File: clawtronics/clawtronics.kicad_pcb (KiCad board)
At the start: 2 copper layers, 81.4 x 87.2 mm, 21 parts, among them J1 TYPE-C-31-M-12, J2 Conn_01x20_Pin, J3 Conn_01x20_Pin, SW1 TS-1088-AR02016, SW2 TS-1088-AR02016, U2 ESP32-S3-WROOM-1, U3 LD1117S33TR_SOT223

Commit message: pcb progress
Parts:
- added C10: 0.1u, Capacitor_SMD:C_0603_1608Metric, F.Cu at (149.5, 76.5)
- added C11: 0.1u, Capacitor_SMD:C_0603_1608Metric, F.Cu at (149.5, 79.0)
- added C12: 0.1u, Capacitor_SMD:C_0603_1608Metric, F.Cu at (149.5, 81.5)
- added C13: 0.1u, Capacitor_SMD:C_0603_1608Metric, F.Cu at (149.5, 84.0)
- added C14: 0.1u, Capacitor_SMD:C_0603_1608Metric, F.Cu at (149.5, 86.5)
- added C15: 0.1u, Capacitor_SMD:C_0603_1608Metric, F.Cu at (153.5, 66.4)
- added C16: 10u, Capacitor_SMD:C_0603_1608Metric, F.Cu at (153.5, 69.0)
- added C17: 0.1u, Capacitor_SMD:C_0603_1608Metric, F.Cu at (153.5, 71.5)
- added C18: 0.1u, Capacitor_SMD:C_0603_1608Metric, F.Cu at (153.5, 74.0)
- added C19: 10u, Capacitor_SMD:C_0603_1608Metric, F.Cu at (153.5, 76.5)
- added C20: 0.022u, Capacitor_SMD:C_0603_1608Metric, F.Cu at (153.5, 79.0)
- added C21: 0.1u, Capacitor_SMD:C_0603_1608Metric, F.Cu at (153.5, 81.5)
- added C22: 0.022u, Capacitor_SMD:C_0603_1608Metric, F.Cu at (153.5, 84.0)
- added C23: 0.022u, Capacitor_SMD:C_0603_1608Metric, F.Cu at (153.5, 86.5)
- added C6: 0.1u, Capacitor_SMD:C_0603_1608Metric, F.Cu at (149.5, 66.4)
- added C7: 0.1u, Capacitor_SMD:C_0603_1608Metric, F.Cu at (149.5, 69.0)
- added C8: 0.1u, Capacitor_SMD:C_0603_1608Metric, F.Cu at (149.5, 71.5)
- added C9: 10u, Capacitor_SMD:C_0603_1608Metric, F.Cu at (149.5, 74.0)
- added J4: Power, Connector_Phoenix_MSTB:PhoenixContact_MSTBV_2,5_6-GF-5,08_1x06_P5.08mm_Vertical_ThreadedFlange_MountHole, F.Cu at (187.5, 78.5)
- added J5: Screw_Terminal_01x06, Connector_Phoenix_MSTB:PhoenixContact_MSTBV_2,5_6-GF-5,08_1x06_P5.08mm_Vertical_ThreadedFlange_MountHole, F.Cu at (122.3, 122.0)
- added R10: 2.74K, Resistor_SMD:R_0603_1608Metric, F.Cu at (157.5, 74.0)
- added R11: 2.21K, Resistor_SMD:R_0603_1608Metric, F.Cu at (157.5, 76.5)
- added R12: 10K, Resistor_SMD:R_0603_1608Metric, F.Cu at (157.5, 79.0)
- added R13: 1K, Resistor_SMD:R_0603_1608Metric, F.Cu at (157.5, 81.5)
- added R14: 2.21K, Resistor_SMD:R_0603_1608Metric, F.Cu at (157.5, 84.0)
- added R15: 10K, Resistor_SMD:R_0603_1608Metric, F.Cu at (157.5, 86.5)
- added R16: 2.74K, Resistor_SMD:R_0603_1608Metric, F.Cu at (161.5, 66.4)
- added R17: 1K, Resistor_SMD:R_0603_1608Metric, F.Cu at (161.5, 69.0)
- added R18: 2.74K, Resistor_SMD:R_0603_1608Metric, F.Cu at (161.5, 71.5)
- added R19: 10K, Resistor_SMD:R_0603_1608Metric, F.Cu at (161.5, 74.0)
- added R20: 10K, Resistor_SMD:R_0603_1608Metric, F.Cu at (161.5, 76.5)
- added R21: 10K, Resistor_SMD:R_0603_1608Metric, F.Cu at (161.5, 79.0)
- added R7: 2.21K, Resistor_SMD:R_0603_1608Metric, F.Cu at (157.5, 66.4)
- added R8: 10K, Resistor_SMD:R_0603_1608Metric, F.Cu at (157.5, 69.0)
- added R9: 1K, Resistor_SMD:R_0603_1608Metric, F.Cu at (157.5, 71.5)
- added U3: DRV8876PWPR, Motors:moto, F.Cu at (181.5, 100.9)
- added U4: DRV8876PWPR, Motors:moto, F.Cu at (167.0, 109.9)
- added U5: DRV8876PWPR, Motors:moto, F.Cu at (145.0, 110.2)
- C1: renamed from C4; value 10u -> 100n
- C5: value 10u -> 1u
- renumbered C1 to C2, C2 to C3, C3 to C4, R2 to R1, R1 to R2, R4 to R3, R5 to R4, R6 to R5, R3 to R6, SW2 to SW1, SW1 to SW2, U2 to U1, U3 to U2

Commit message: figured out switches
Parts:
- removed J1: TYPE-C-31-M-12, TYPE-C-31-M-12:HRO_TYPE-C-31-M-12
- added D4: 1N4001, Diode_THT:D_DO-41_SOD81_P10.16mm_Horizontal, F.Cu at (60.6, 66.6)
- added J6: Screw_Terminal_01x09, TerminalBlock:TerminalBlock_MaiXu_MX126-5.0-09P_1x09_P5.00mm, F.Cu at (30.7, 31.6)
- added J7: Screw_Terminal_01x15, TerminalBlock:TerminalBlock_MaiXu_MX126-5.0-15P_1x15_P5.00mm, F.Cu at (21.5, 21.5)
- added J8: Screw_Terminal_01x02, TerminalBlock:TerminalBlock_MaiXu_MX126-5.0-02P_1x02_P5.00mm, F.Cu at (62.8, 73.7)
- added Q1: AO3400A, Package_TO_SOT_SMD:SOT-23, F.Cu at (75.1, 66.7)
- added R22: 1K, Resistor_SMD:R_0603_1608Metric, F.Cu at (44.7, 63.6)
- added R23: 1K, Resistor_SMD:R_0603_1608Metric, F.Cu at (44.7, 66.1)
- added R24: 1K, Resistor_SMD:R_0603_1608Metric, F.Cu at (44.7, 68.6)
- added R25: 1K, Resistor_SMD:R_0603_1608Metric, F.Cu at (44.7, 71.1)
- added R26: 1K, Resistor_SMD:R_0603_1608Metric, F.Cu at (44.7, 73.6)
- added R27: 660, Resistor_SMD:R_0603_1608Metric, F.Cu at (44.7, 76.2)
- added R28: 220, Resistor_SMD:R_0603_1608Metric, F.Cu at (44.7, 78.7)
- added R29: 10K, Resistor_SMD:R_0603_1608Metric, F.Cu at (44.7, 81.2)
- J2, J3: moved to F.Cu
- J4, J5: footprint Connector_Phoenix_MSTB:PhoenixContact_MSTBV_2,5_6-GF-5,08_1x06_P5.08mm_Vertical_ThreadedFlange_MountHole -> TerminalBlock_MetzConnect:TerminalBlock_MetzConnect_Type011_RT05506HBLC_1x06_P5.00mm_Horizontal
- SW1, SW2: footprint easyeda2kicad:SW-SMD_L3.9-W3.0-P4.45 -> Button_Switch_SMD:SW_SPST_TS-1088-xR020
- moved J4 161.0 mm to (30.2, 44.2), turned to 0 degrees
- moved U3 134.6 mm to (51.6, 65.6)
- moved R10 121.7 mm to (36.7, 88.7)
- moved R7 121.7 mm to (36.7, 81.2)
- moved R8 121.7 mm to (36.7, 83.7)
- moved R9 121.7 mm to (36.7, 86.2)
- moved U4 121.4 mm to (51.6, 72.2)
- moved C10 121.2 mm to (28.7, 86.2)
- moved C11 121.2 mm to (28.7, 88.7)
- moved C6 121.2 mm to (28.7, 76.2)
- moved C7 121.2 mm to (28.7, 78.7)
- moved C8 121.2 mm to (28.7, 81.2)
- moved C9 121.2 mm to (28.7, 83.7)
- moved R16 121.2 mm to (40.7, 76.2)
- moved R17 121.2 mm to (40.7, 78.7)
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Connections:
- C14 pad 2: Net-(U3-VREF) -> Net-(U5-VREF)
- C17 pad 1: Net-(U3-VCP) -> Net-(U5-VCP)
- C20 pad 1: Net-(U5-CPH) -> Net-(U3-CPH)
- C20 pad 2: Net-(U5-CPL) -> Net-(U3-CPL)
- C23 pad 1: Net-(U3-CPH) -> Net-(U5-CPH)
- C23 pad 2: Net-(U3-CPL) -> Net-(U5-CPL)
- C7 pad 2: Net-(U5-VREF) -> Net-(U3-VREF)
- C8 pad 1: Net-(U5-VCP) -> Net-(U3-VCP)
- R10 pad 1: Net-(U5-IPROPI) -> Net-(U3-IPROPI)
- R14 pad 2: Net-(U3-VREF) -> Net-(U5-VREF)
- R15 pad 1: Net-(U3-VREF) -> Net-(U5-VREF)
- R17 pad 2: Net-(U3-IPROPI) -> Net-(U5-IPROPI)
- R18 pad 1: Net-(U3-IPROPI) -> Net-(U5-IPROPI)
- R7 pad 2: Net-(U5-VREF) -> Net-(U3-VREF)
- R8 pad 1: Net-(U5-VREF) -> Net-(U3-VREF)
- R9 pad 2: Net-(U5-IPROPI) -> Net-(U3-IPROPI)
- U3 pad 1: GPIO1 -> GPIO9
- U3 pad 10: Net-(J5-Pin_2) -> Net-(J5-Pin_6)
- U3 pad 2: GPIO2 -> GPIO10
- U3 pad 3: +3V3 -> +3.3V
- U3 pad 8: Net-(J5-Pin_1) -> Net-(J5-Pin_5)
- U5 pad 1: GPIO9 -> GPIO1
- U5 pad 10: Net-(J5-Pin_6) -> Net-(J5-Pin_2)
- U5 pad 2: GPIO10 -> GPIO2
- U5 pad 3: +3.3V -> +3V3
- U5 pad 8: Net-(J5-Pin_5) -> Net-(J5-Pin_1)
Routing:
- net GND: track 114.6 -> 0.00 mm, vias 38 -> 0
- net +5V: track 70.1 -> 0.00 mm, vias 3 -> 0
- net +3V3: track 61.6 -> 0.00 mm, vias 2 -> 0
- net EN: track 59.4 -> 0.00 mm, vias 3 -> 0
- net D-: track 56.2 -> 0.00 mm, vias 2 -> 0
- net D+: track 56.1 -> 0.00 mm, vias 3 -> 0
- net GPIO12: track 36.1 -> 0.00 mm
- net GPIO13: track 35.7 -> 0.00 mm, vias 1 -> 0
- net GPIO0: track 35.3 -> 0.00 mm, vias 1 -> 0
- net GPIO11: track 32.6 -> 0.00 mm
- net GPIO14: track 32.6 -> 0.00 mm, vias 1 -> 0
- net GPIO21: track 30.5 -> 0.00 mm, vias 1 -> 0
- net GPIO10: track 29.6 -> 0.00 mm
- net GPIO9: track 26.5 -> 0.00 mm
- net GPIO47: track 26.5 -> 0.00 mm, vias 1 -> 0
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- removed copper zone on B.Cu, net GND
- removed copper zone on F.Cu, net GND
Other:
- board outline removed
- board text removed: "0"
- board text removed: "1"
- board text removed: "10"
- board text removed: "11"
- board text removed: "12"
- board text removed: "13"
- board text removed: "14"
- board text removed: "15"
- board text removed: "16"
- board text removed: "17"
- board text removed: "18"
- board text removed: "19"
- board text removed: "2"
- board text removed: "20"
- board text removed: "21"
- board text removed: "3"
- board text removed: "35"
- board text removed: "36"
- board text removed: "37"
- board text removed: "38"
- board text removed: "39"
- board text removed: "3V3"
- board text removed: "4"
- board text removed: "40"
- board text removed: "41"
- board text removed: "42"
- board text removed: "43"
- board text removed: "44"
- board text removed: "45"
- board text removed: "46"
- board text removed: "47"
- board text removed: "48"
- board text removed: "5"
- board text removed: "5V"
- board text removed: "6"
- board text removed: "7"
- board text removed: "8"
- board text removed: "9"
- board text removed: "BOOT"
- board text removed: "Clawtronics"
- board text removed: "EN"
- board text removed: "GND"
- board text removed: "RESET"

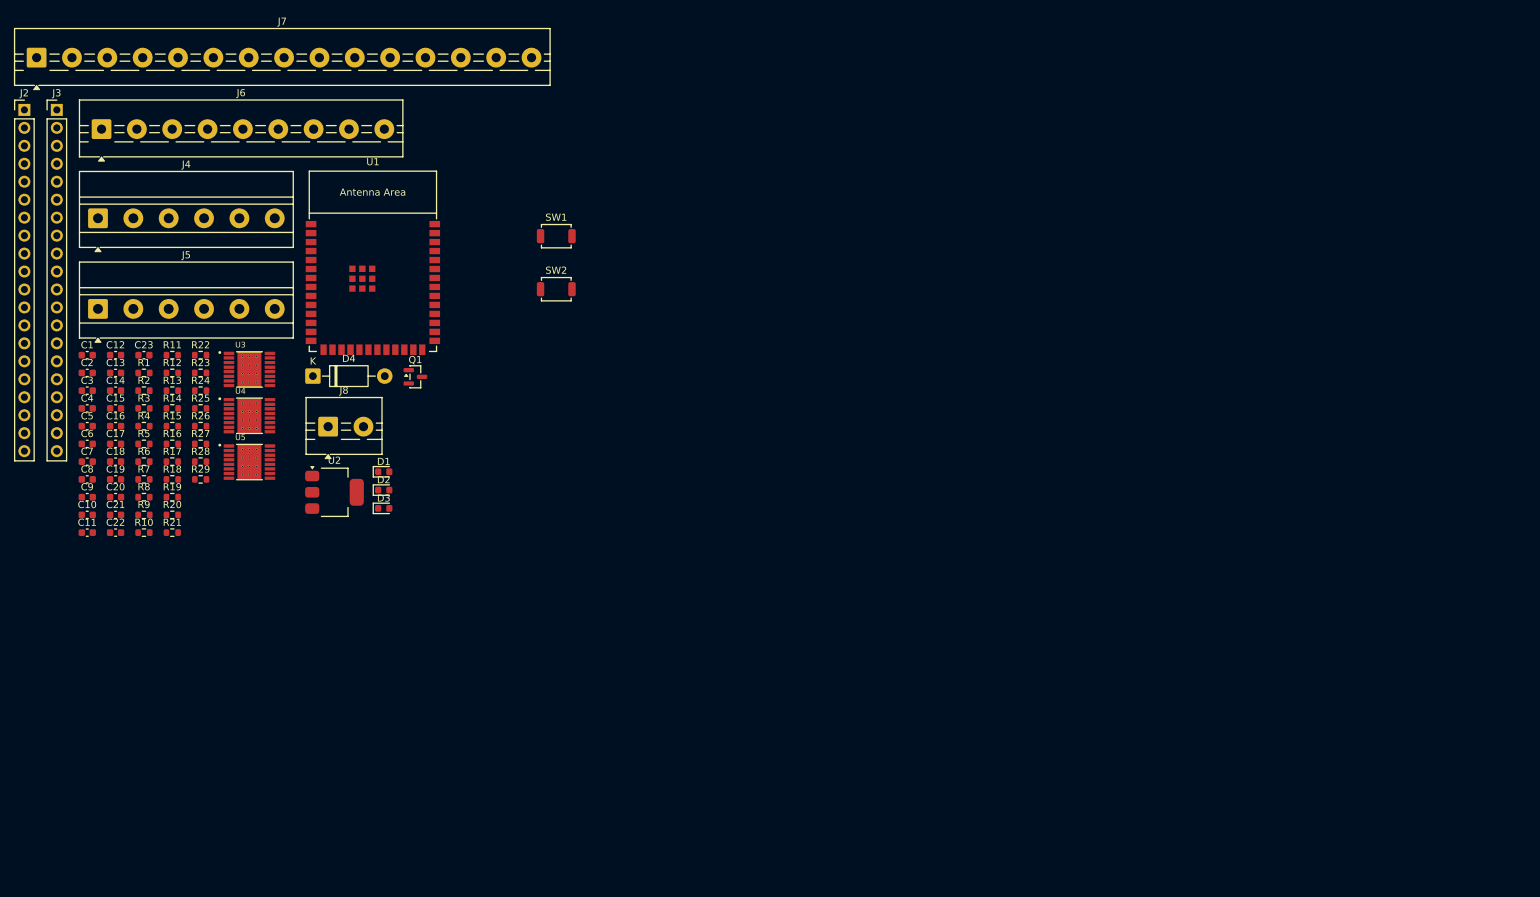
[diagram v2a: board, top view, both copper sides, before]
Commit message: layout with hierarchical sheets
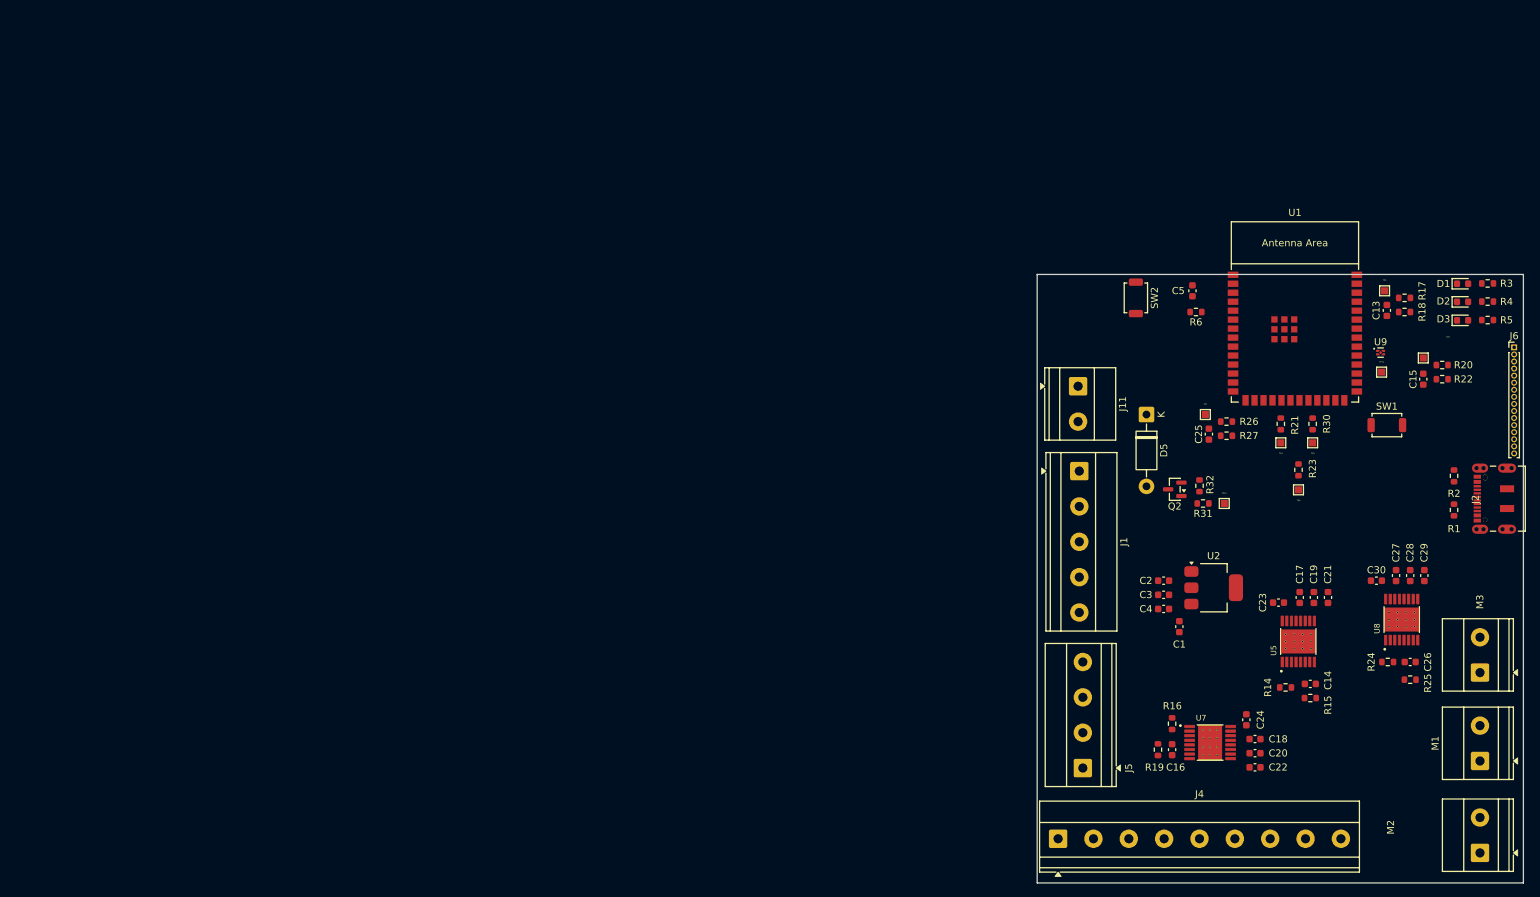
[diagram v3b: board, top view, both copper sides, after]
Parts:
- removed C10, C11, C12, C6, C7, C8: 0.1u, Capacitor_SMD:C_0603_1608Metric
- removed C9: 10u, Capacitor_SMD:C_0603_1608Metric
- removed D4: 1N4001, Diode_THT:D_DO-41_SOD81_P10.16mm_Horizontal
- removed J3: Conn_01x20_Pin, Connector_PinHeader_2.54mm:PinHeader_1x20_P2.54mm_Vertical
- removed J7: Screw_Terminal_01x15, TerminalBlock:TerminalBlock_MaiXu_MX126-5.0-15P_1x15_P5.00mm
- removed J8: Screw_Terminal_01x02, TerminalBlock:TerminalBlock_MaiXu_MX126-5.0-02P_1x02_P5.00mm
- removed Q1: AO3400A, Package_TO_SOT_SMD:SOT-23
- removed R10: 2.74K, Resistor_SMD:R_0603_1608Metric
- removed R11, R7: 2.21K, Resistor_SMD:R_0603_1608Metric
- removed R12, R29, R8: 10K, Resistor_SMD:R_0603_1608Metric
- removed R13, R9: 1K, Resistor_SMD:R_0603_1608Metric
- removed R28: 220, Resistor_SMD:R_0603_1608Metric
- removed U3, U4: DRV8876PWPR, Motors:moto
- added C24: 0.022u, Capacitor_SMD:C_0603_1608Metric, F.Cu at (192.6, 115.2)
- added C25: 0.1u, Capacitor_SMD:C_0603_1608Metric, F.Cu at (187.3, 74.8)
- added C26: 0.1u, Capacitor_SMD:C_0603_1608Metric, F.Cu at (215.8, 107.0)
- added C27: 0.1u, Capacitor_SMD:C_0603_1608Metric, F.Cu at (213.8, 94.8)
- added C28: 10u, Capacitor_SMD:C_0603_1608Metric, F.Cu at (215.8, 94.8)
- added C29: 0.1u, Capacitor_SMD:C_0603_1608Metric, F.Cu at (217.8, 94.8)
- added C30: 0.022u, Capacitor_SMD:C_0603_1608Metric, F.Cu at (211.0, 95.5)
- added D5: 1N4001, Diode_THT:D_DO-41_SOD81_P10.16mm_Horizontal, F.Cu at (178.5, 72.0)
- added J1: Screw_Terminal_01x05, TerminalBlock_Phoenix:TerminalBlock_Phoenix_MKDS-1,5-5_1x05_P5.00mm_Horizontal, F.Cu at (169.0, 80.0)
- added J11: Screw_Terminal_01x02, TerminalBlock_Phoenix:TerminalBlock_Phoenix_MKDS-1,5-2_1x02_P5.00mm_Horizontal, F.Cu at (168.8, 68.0)
- added M1: Motor_DC, TerminalBlock_Phoenix:TerminalBlock_Phoenix_MKDS-1,5-2_1x02_P5.00mm_Horizontal, F.Cu at (225.7, 121.0)
- added M2: Motor_DC, TerminalBlock_Phoenix:TerminalBlock_Phoenix_MKDS-1,5-2_1x02_P5.00mm_Horizontal, F.Cu at (225.7, 134.0)
- added M3: Motor_DC, TerminalBlock_Phoenix:TerminalBlock_Phoenix_MKDS-1,5-2_1x02_P5.00mm_Horizontal, F.Cu at (225.7, 108.5)
- added Q2: AO3400A, Package_TO_SOT_SMD:SOT-23, F.Cu at (182.5, 82.6)
- added R30: 10K, Resistor_SMD:R_0603_1608Metric, F.Cu at (202.0, 73.3)
- added R31: 220, Resistor_SMD:R_0603_1608Metric, F.Cu at (186.5, 84.6)
- added R32: 10K, Resistor_SMD:R_0603_1608Metric, F.Cu at (186.0, 82.1)
- added TP11: TestPoint, TestPoint:TestPoint_Pad_1.0x1.0mm, F.Cu at (211.8, 66.0)
- added TP12: TestPoint, TestPoint:TestPoint_Pad_1.0x1.0mm, F.Cu at (189.5, 84.6)
- added TP3: TestPoint, TestPoint:TestPoint_Pad_1.0x1.0mm, F.Cu at (212.2, 54.5)
- added TP4: TestPoint, TestPoint:TestPoint_Pad_1.0x1.0mm, F.Cu at (197.5, 76.0)
- added TP5: TestPoint, TestPoint:TestPoint_Pad_1.0x1.0mm, F.Cu at (217.7, 64.0)
- added TP6: TestPoint, TestPoint:TestPoint_Pad_1.0x1.0mm, F.Cu at (200.0, 82.7)
- added TP7: TestPoint, TestPoint:TestPoint_Pad_1.0x1.0mm, F.Cu at (186.8, 72.0)
- added TP9: TestPoint, TestPoint:TestPoint_Pad_1.0x1.0mm, F.Cu at (202.0, 76.0)
- added U7: DRV8876PWPR, Motors:moto, F.Cu at (187.5, 118.4)
- added U8: DRV8876PWPR, Motors:moto, F.Cu at (214.6, 101.0)
- added U9: 74LVC1G17, Package_SON:Texas_X2SON-5_0.8x0.8mm_P0.48mm, F.Cu at (211.6, 63.2)
- C16: value 10u -> 0.1u
- C20: value 0.022u -> 10u
- C22: value 0.022u -> 0.1u
- J2: value Conn_01x20_Pin -> DX07S016JA3R1500; footprint Connector_PinHeader_2.54mm:PinHeader_1x20_P2.54mm_Vertical -> clawtronics:CONN12_DX07S_JAE
- J4: value Power -> Screw_Terminal_01x09; footprint TerminalBlock_MetzConnect:TerminalBlock_MetzConnect_Type011_RT05506HBLC_1x06_P5.00mm_Horizontal -> TerminalBlock_Phoenix:TerminalBlock_Phoenix_MKDS-1,5-9_1x09_P5.00mm_Horizontal
- J5: value Screw_Terminal_01x06 -> Screw_Terminal_01x04; footprint TerminalBlock_MetzConnect:TerminalBlock_MetzConnect_Type011_RT05506HBLC_1x06_P5.00mm_Horizontal -> TerminalBlock_Phoenix:TerminalBlock_Phoenix_MKDS-1,5-4_1x04_P5.00mm_Horizontal
- J6: value Screw_Terminal_01x09 -> Conn_01x16_Pin; footprint TerminalBlock:TerminalBlock_MaiXu_MX126-5.0-09P_1x09_P5.00mm -> Connector_PinHeader_1.00mm:PinHeader_1x16_P1.00mm_Vertical
- R16: value 2.74K -> 2.21K
- R20: value 10K -> 1K
- R22: value 1K -> 2.74K
- R23, R25: value 1K -> 10K
- R24: value 1K -> 2.21K
- R27: value 660 -> 2.74K
- SW1, SW2: value TS-1088-AR02016 -> SW_SPST_TS-1088-xR020
- moved J2 215.8 mm to (228.5, 83.9), turned to 90 degrees
- moved J6 202.2 mm to (230.5, 62.5)
- moved R3 190.9 mm to (226.8, 53.5), turned to 180 degrees
- moved R4 190.9 mm to (226.8, 56.0), turned to 180 degrees
- moved R5 190.9 mm to (226.8, 58.6), turned to 180 degrees
- moved R1 186.3 mm to (222.0, 85.5), turned to -90 degrees
- moved R2 185.7 mm to (222.0, 80.7), turned to 90 degrees
- moved C15 185.0 mm to (217.7, 67.0), turned to 90 degrees
- moved R20 180.9 mm to (220.3, 65.0)
- moved C13 180.0 mm to (212.5, 57.3), turned to -90 degrees
- moved R18 175.9 mm to (215.0, 57.5)
- moved R17 175.8 mm to (215.0, 55.5), turned to 180 degrees
- moved R22 175.6 mm to (220.3, 67.0), turned to 180 degrees
- moved R25 175.3 mm to (215.8, 109.5)
- moved C14 174.0 mm to (201.7, 110.1), turned to 180 degrees
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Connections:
- C13 pad 2: GPIO3 -> /motors/IPROPI
- C15 pad 1: Net-(U4-VCP) -> GND
- C15 pad 2: +24V -> /motors1/IPROPI
- C16 pad 2: +24V -> Net-(U7-VREF)
- C18 pad 1: GND -> Net-(U7-VCP)
- C20 pad 1: Net-(U3-CPH) -> GND
- C20 pad 2: Net-(U3-CPL) -> +24V
- C22 pad 1: Net-(U4-CPH) -> GND
- C22 pad 2: Net-(U4-CPL) -> +24V
- J2 pad 10: GPIO17 -> unconnected-(J2-SBU1-Pad10)
- J2 pad 11: GPIO18 -> +5V
- J2 pad 12: GPIO8 -> GND
- J2 pad 13: D- -> (no net)
- J2 pad 14: D+ -> (no net)
- J2 pad 15: GPIO3 -> (no net)
- J2 pad 16: GPIO46 -> (no net)
- J2 pad 17: GPIO9 -> (no net)
- J2 pad 18: GPIO10 -> (no net)
- J2 pad 19: GPIO11 -> (no net)
- J2 pad 2: +3V3 -> +5V
- J2 pad 3: EN -> Net-(J2-CC1)
- J2 pad 4: GPIO4 -> unconnected-(J2-SBU2-Pad4)
- J2 pad 5: GPIO5 -> D-
- J2 pad 6: GPIO6 -> D+
- J2 pad 7: GPIO7 -> D+
- J2 pad 8: GPIO15 -> D-
- J2 pad 9: GPIO16 -> Net-(J2-CC2)
- J4 pad 1: +24V -> Net-(J4-Pin_1)
- J4 pad 2: GND -> /switches/Pulse2
- J4 pad 3: +12V -> /switches/Pulse3
- J4 pad 4: GND -> /switches/DoorOpen
- J4 pad 5: +5V -> /switches/PulseInhibit
- J4 pad 6: GND -> +5V
- J5 pad 1: Net-(J5-Pin_1) -> +24V
- J5 pad 2: Net-(J5-Pin_2) -> +12V
- J5 pad 3: Net-(J5-Pin_3) -> +5V
- J5 pad 4: Net-(J5-Pin_4) -> GNDPWR
- J6 pad 1: GPIO11 -> +5V
- J6 pad 2: GND -> +3V3
- J6 pad 3: GPIO12 -> GPIO43
- J6 pad 4: GND -> GPIO44
- J6 pad 5: GPIO13 -> GPIO42
- J6 pad 6: GND -> GPIO41
- J6 pad 7: GND -> GPIO40
- J6 pad 8: GND -> GPIO39
- J6 pad 9: GPIO17 -> GPIO37
- R1 pad 1: Net-(J1-CC1) -> Net-(J2-CC1)
- R16 pad 1: Net-(U4-IPROPI) -> +3V3
- R16 pad 2: GND -> Net-(U7-VREF)
- R17 pad 1: GPIO3 -> /motors/IPROPI
- R19 pad 1: +3V3 -> Net-(U7-VREF)
- R19 pad 2: GPIO21 -> GND
- R2 pad 1: Net-(J1-CC2) -> Net-(J2-CC2)
- R20 pad 1: +3V3 -> /motors1/IPROPI
- R20 pad 2: GPIO21 -> Net-(U7-IPROPI)
- R21 pad 2: GPIO21 -> /motors/NFAULT
- R22 pad 1: +3V3 -> Net-(U7-IPROPI)
- R22 pad 2: GPIO17 -> GND
- R23 pad 2: GPIO13 -> /motors1/NFAULT
- R24 pad 2: GPIO11 -> Net-(U8-VREF)
- R25 pad 1: +3V3 -> Net-(U8-VREF)
- R25 pad 2: GPIO12 -> GND
- R26 pad 1: +5V -> /motors2/IPROPI
- R26 pad 2: GPIO45 -> Net-(U8-IPROPI)
- R27 pad 1: GPIO45 -> Net-(U8-IPROPI)
- R5 pad 1: GPIO21 -> GPIO44
- U1 pad 10: GPIO17 -> /switches/Pulse3
- U1 pad 11: GPIO18 -> /switches/Grip
- U1 pad 12: GPIO8 -> /motors1/EN/IN1
- U1 pad 15: GPIO3 -> /motors2/IPROPI
- U1 pad 16: GPIO46 -> /motors2/DIR/IN2
- U1 pad 17: GPIO9 -> /motors/EN/IN1
- U1 pad 18: GPIO10 -> /motors1/DIR/IN2
- U1 pad 19: GPIO11 -> /motors/DIR/IN2
- U1 pad 20: GPIO12 -> /motors/NFAULT
- U1 pad 21: GPIO13 -> /motors1/NFAULT
- U1 pad 22: GPIO14 -> /motors2/NFAULT
- U1 pad 23: GPIO21 -> /switches/Pulse2
- U1 pad 24: GPIO47 -> /switches/PulseInhibit
- U1 pad 25: GPIO48 -> /switches/DoorOpen
- U1 pad 26: GPIO45 -> /motors2/EN/IN1
- U1 pad 31: GPIO38 -> /switches/Pulse1
- U1 pad 38: GPIO2 -> /motors1/IPROPI
- U1 pad 39: GPIO1 -> /motors/IPROPI
- U1 pad 4: GPIO4 -> /switches/Fused
- U1 pad 5: GPIO5 -> /switches/MaxY
- U1 pad 6: GPIO6 -> /switches/MinY
- U1 pad 7: GPIO7 -> /switches/MinX
- U5 pad 1: GPIO1 -> /motors/EN/IN1
- U5 pad 10: Net-(J5-Pin_2) -> Net-(M1--)
- U5 pad 2: GPIO2 -> /motors/DIR/IN2
- U5 pad 4: GPIO21 -> /motors/NFAULT
- U5 pad 8: Net-(J5-Pin_1) -> Net-(M1-+)
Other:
- board outline added: 68.8 x 86.1 mm

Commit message: layout so far
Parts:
- moved C28 2.20 mm to (218.0, 94.8)
- moved C29 2.20 mm to (220.0, 94.8)
- moved R1 2.00 mm to (222.0, 87.5)
- moved R14 1.48 mm to (196.8, 110.0)
- moved R24 1.30 mm to (211.3, 107.0)
- moved R2 1.17 mm to (222.0, 79.5)
- moved C20 1.10 mm to (193.8, 121.0)
- moved C22 1.10 mm to (193.8, 123.0)
- moved J4 1.00 mm to (167.0, 132.0)
- moved C24 0.88 mm to (193.5, 115.2)
- moved C26 0.86 mm to (216.5, 107.5)
- moved R25 0.86 mm to (216.5, 110.0)
- moved C19 0.82 mm to (203.0, 97.9)
- moved C21 0.82 mm to (205.0, 97.9)
- moved R16 0.66 mm to (181.5, 115.5)
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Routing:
- net GND: track 0.00 -> 126.7 mm, vias 0 -> 17
- net Net-(U7-IPROPI): track 0.00 -> 81.6 mm, vias 0 -> 4
- net +24V: track 0.00 -> 71.6 mm, vias 0 -> 3
- net Net-(U5-IPROPI): track 0.00 -> 66.9 mm, vias 0 -> 5
- net /motors1/DIR/IN2: track 0.00 -> 60.0 mm, vias 0 -> 3
- net Net-(U8-IPROPI): track 0.00 -> 59.2 mm, vias 0 -> 6
- net +12V: track 0.00 -> 58.4 mm, vias 0 -> 2
- net /motors1/EN/IN1: track 0.00 -> 55.2 mm, vias 0 -> 3
- net /motors1/NFAULT: track 0.00 -> 52.6 mm, vias 0 -> 4
- net /motors2/DIR/IN2: track 0.00 -> 52.1 mm, vias 0 -> 4
- net /motors2/NFAULT: track 0.00 -> 48.5 mm, vias 0 -> 4
- net Net-(M2-+): track 0.00 -> 46.8 mm, vias 0 -> 1
- net /motors/DIR/IN2: track 0.00 -> 46.8 mm, vias 0 -> 4
- net /motors/NFAULT: track 0.00 -> 43.7 mm, vias 0 -> 2
- net /motors/EN/IN1: track 0.00 -> 43.5 mm, vias 0 -> 4
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- added copper zone on In1.Cu, net GND
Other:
- copper layers 2 -> 4

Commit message: finished layout
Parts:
- U9: footprint Package_SON:Texas_X2SON-5_0.8x0.8mm_P0.48mm -> Package_SON:Texas_X2SON-5_0.8x0.8mm_P0.48mm_RoutingVia
- moved J2 68.4 mm to (165.8, 56.4), turned to -90 degrees
- moved R1 59.5 mm to (173.5, 53.0), turned to 90 degrees
- moved R2 55.8 mm to (171.5, 55.8), turned to -90 degrees
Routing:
- net +5V: track 22.3 -> 214.8 mm, vias 2 -> 6
- net /switches/DoorOpen: track 0.00 -> 108.5 mm
- net Net-(J4-Pin_1): track 0.00 -> 104.4 mm, vias 0 -> 2
- net /switches/Pulse2: track 0.00 -> 90.6 mm
- net /switches/Pulse3: track 0.00 -> 81.6 mm
- net GND: track 126.7 -> 207.9 mm, vias 17 -> 27
- net GNDPWR: track 3.00 -> 81.8 mm
- net /switches/PulseInhibit: track 0.00 -> 75.9 mm
- net +24V: track 71.6 -> 146.4 mm
- net /switches/MaxY: track 0.00 -> 69.9 mm
- net EN: track 0.00 -> 68.7 mm, vias 0 -> 4
- net /switches/MinY: track 0.00 -> 61.9 mm
- net /switches/Fused: track 0.00 -> 60.7 mm
- net GPIO16: track 0.00 -> 53.9 mm, vias 0 -> 1
- net /switches/MinX: track 0.00 -> 50.4 mm
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- added copper zone on In2.Cu, net +3V3
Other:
- board size 68.8 x 86.1 mm -> 68.5 x 87.6 mm

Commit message: made geber files
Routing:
- net +3V3: track 56.1 -> 76.7 mm, vias 10 -> 12
- net GND: track 207.9 -> 223.4 mm, vias 27 -> 34
